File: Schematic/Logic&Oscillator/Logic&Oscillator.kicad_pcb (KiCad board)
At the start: 2 copper layers, 116.8 x 50.8 mm, 36 parts, among them J1 KLDVHCX-0202-A, J2 KLDVHCX-0202-A, J3 RJ45-Unshielded, J4 RJ45-Unshielded, Q1 VN3205, U1 ICM7555, U2 ARDUINO_Pro-Mini 5v, U3 uA9638C, U4 uA9638C, U5 DS8921

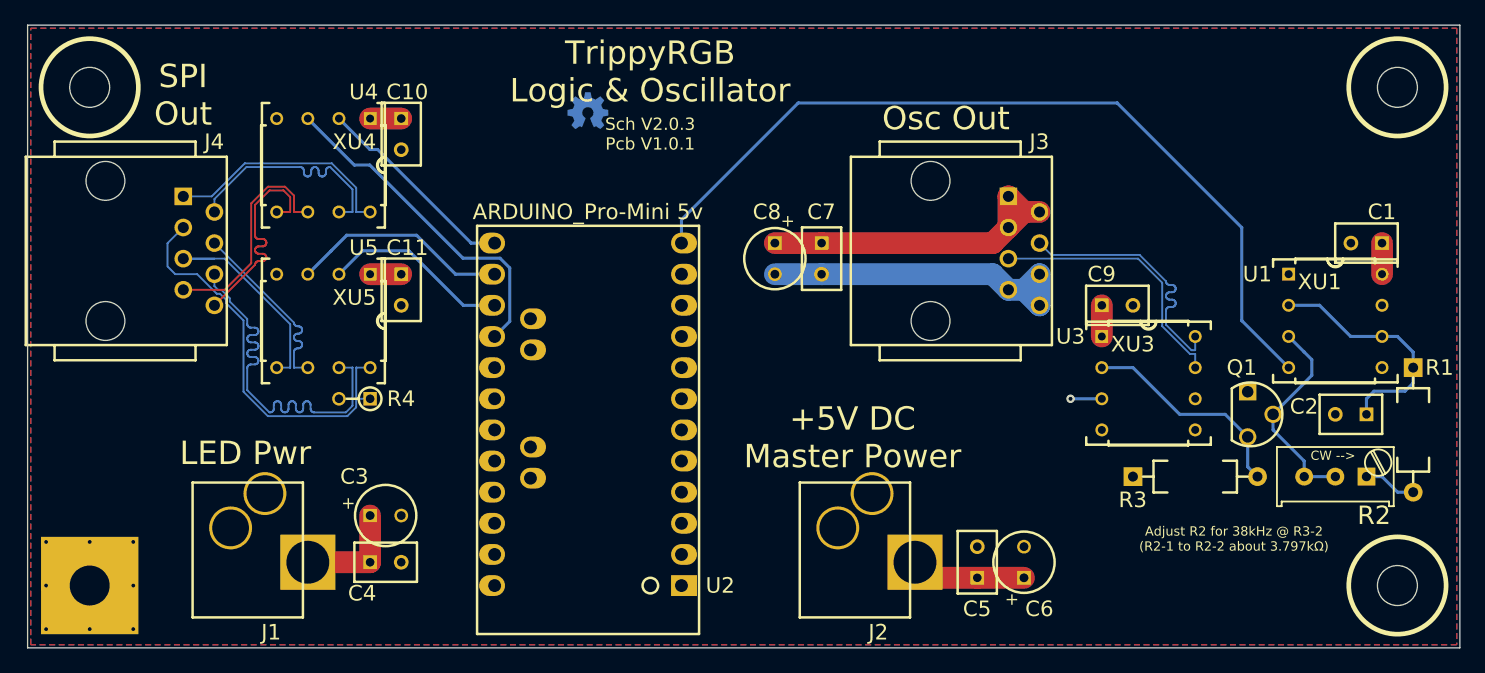
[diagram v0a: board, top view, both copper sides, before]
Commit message: KiCAD upgrade
Upgrade schematic and pcb files for KiCad v5.
Make 8-pin dip holes larger for crimped-pin sockets
InteractiveBOM plugin v1.1 board stuffing files generated.
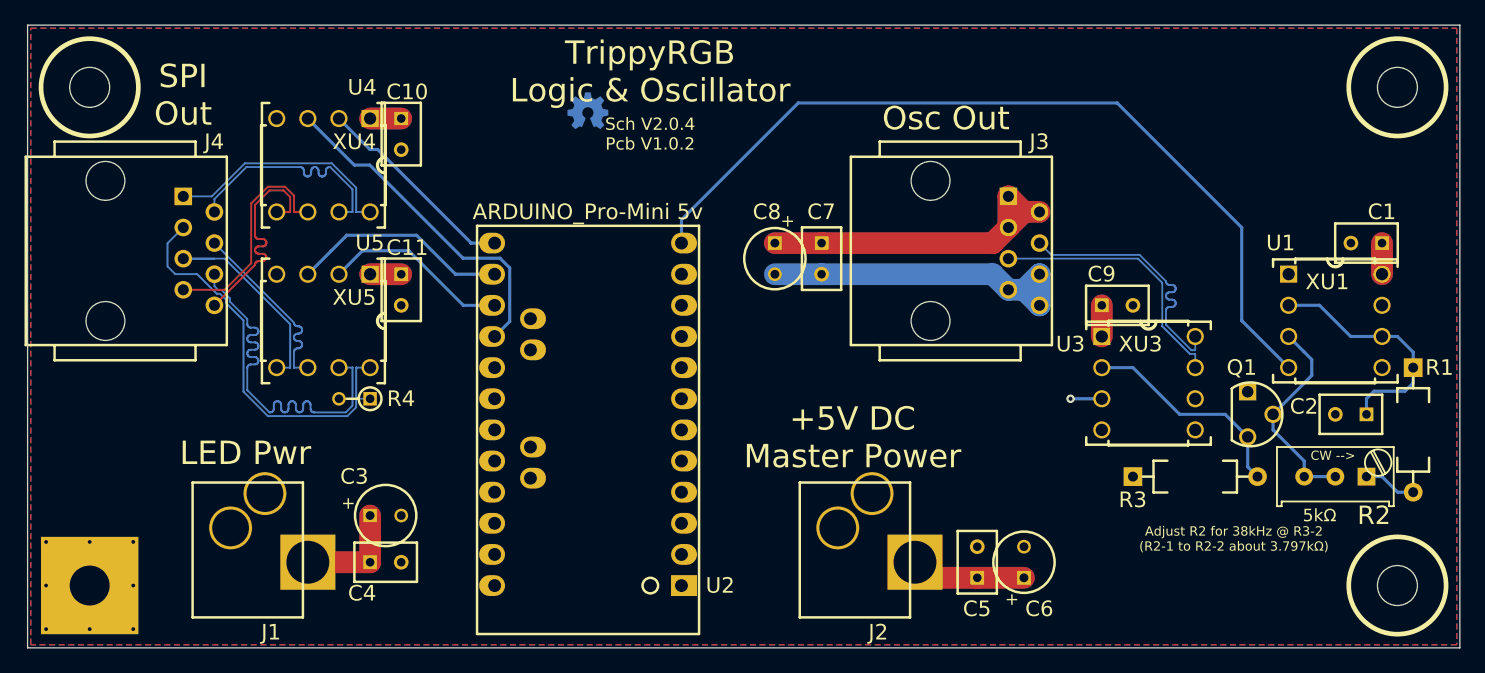
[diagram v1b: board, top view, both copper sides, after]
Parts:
- turned U1 to 0 degrees
- turned U3 to 0 degrees
- turned U4 to 270 degrees
- turned U5 to 270 degrees
- turned XU1 to 0 degrees
- turned XU3 to 0 degrees
- turned XU4 to 270 degrees
- turned XU5 to 270 degrees
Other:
- rule pad_to_mask_clearance: 0 -> 0.0508
- board text added: "Sch V2.0.4 Pcb V1.0.2"
- board text removed: "Sch V2.0.3 Pcb V1.0.1"
